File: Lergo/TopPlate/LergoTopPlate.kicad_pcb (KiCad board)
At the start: 2 copper layers, 164 x 146.3 mm, 39 parts, among them SW2 KEY_SWITCH, SW2 PRO MICRO

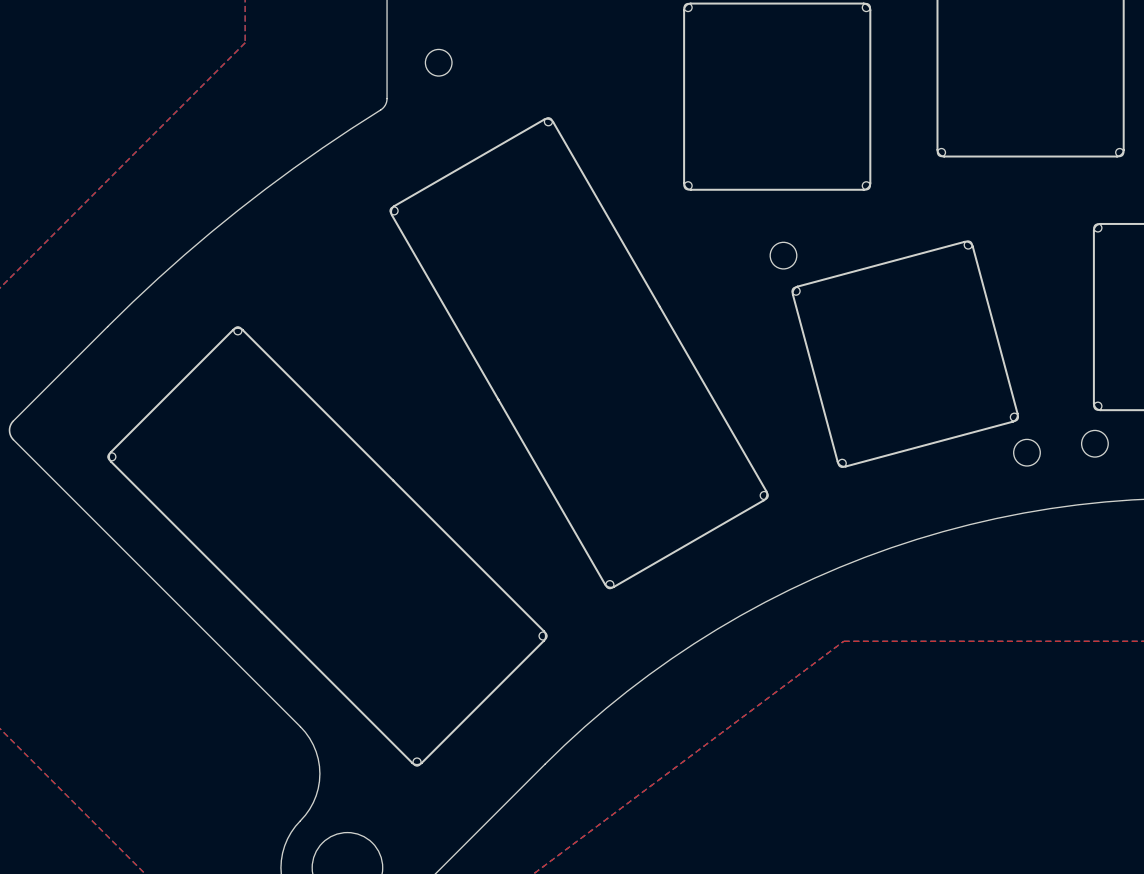
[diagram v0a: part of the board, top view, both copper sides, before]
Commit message: Integrating Pimoroni trackball in all top plates.
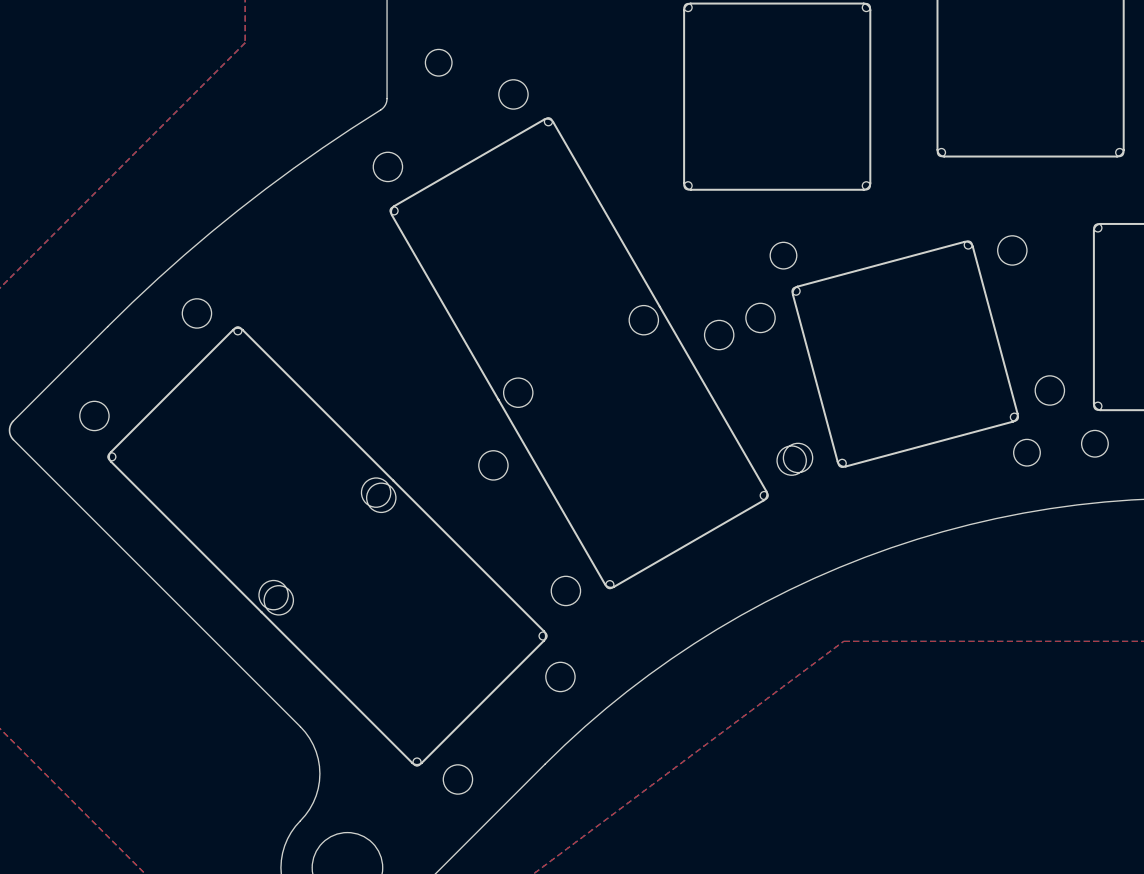
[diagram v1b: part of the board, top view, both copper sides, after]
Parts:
- added REF**: Pimoroni_Trackball, Lergo Footprints:Pimoroni_Trackball, F.Cu at (90.4, 128.6)
- added REF**: Pimoroni_Trackball, Lergo Footprints:Pimoroni_Trackball, F.Cu at (111.3, 112.6)
- added REF**: Pimoroni_Trackball, Lergo Footprints:Pimoroni_Trackball, F.Cu at (103.9, 142.1)
- added REF**: Pimoroni_Trackball, Lergo Footprints:Pimoroni_Trackball, F.Cu at (120.8, 129.1)
- added REF**: Pimoroni_Trackball, Lergo Footprints:Pimoroni_Trackball, F.Cu at (140.6, 120.9)

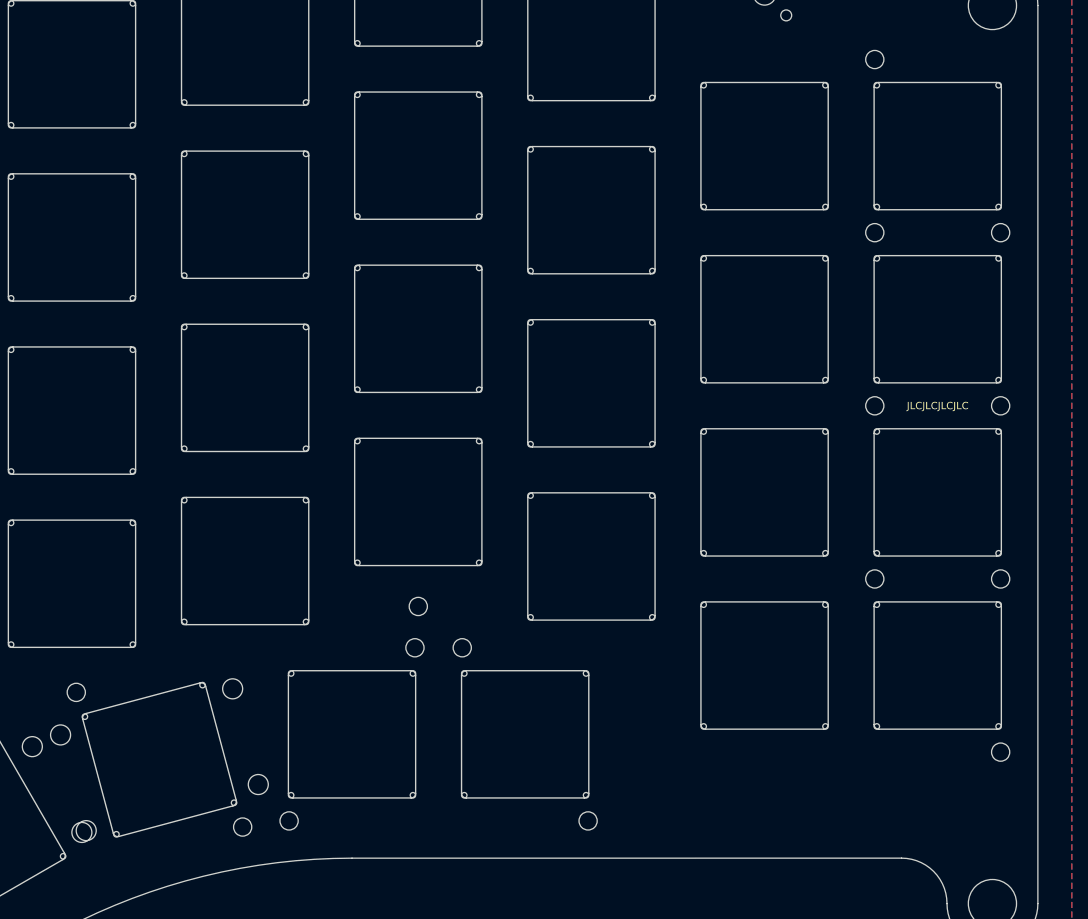
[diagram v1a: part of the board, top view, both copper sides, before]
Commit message: Extended silkscreen for roller encoder on all pre-drilled encoder positions.
Also, doubled the pre-drills rotated 90 degrees for easier mounting of roller encoder in alternate direction.
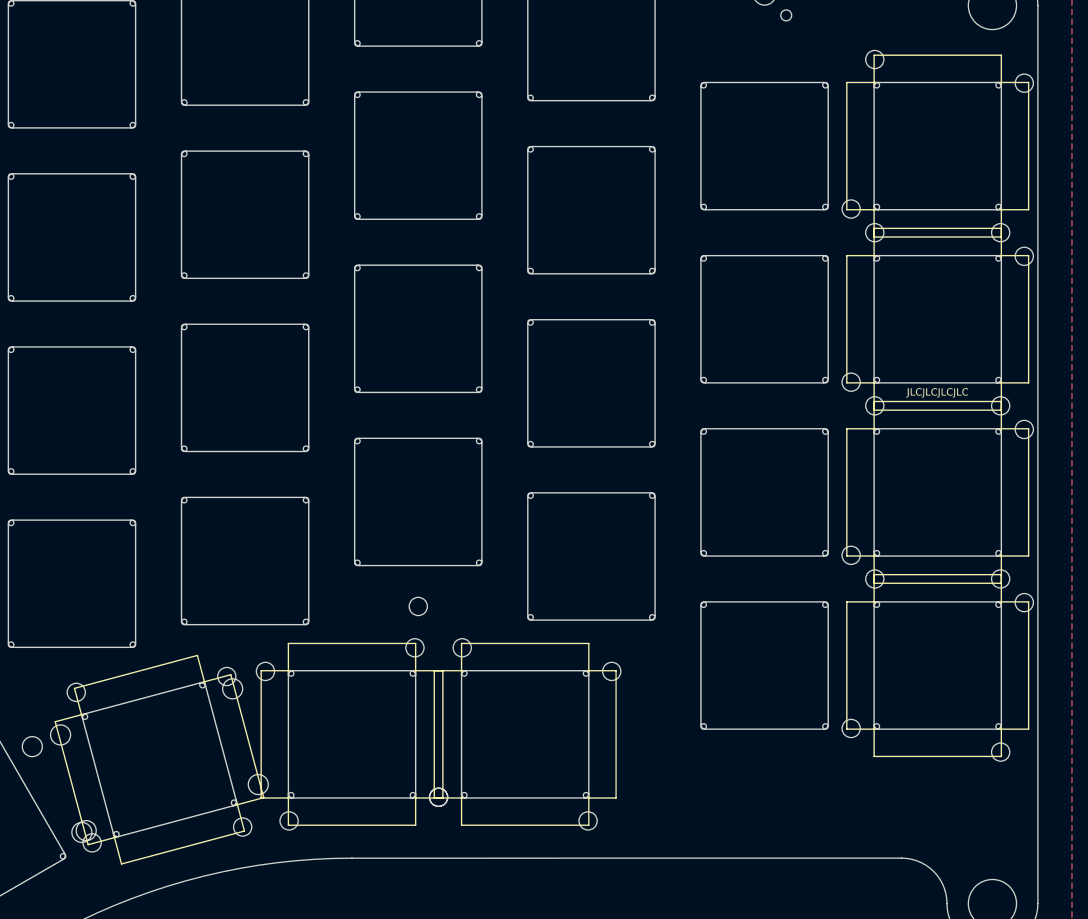
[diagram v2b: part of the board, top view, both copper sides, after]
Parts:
- added REF**: RollerEncoder_Panasonic_EVQWGD001, Lergo Footprints:RollerEncoder_TopPlate, F.Cu at (140.6, 120.9)
- added REF**: RollerEncoder_Panasonic_EVQWGD001, Lergo Footprints:RollerEncoder_TopPlate, F.Cu at (226.2, 53.4)
- added REF**: RollerEncoder_Panasonic_EVQWGD001, Lergo Footprints:RollerEncoder_TopPlate, F.Cu at (226.2, 72.5)
- added REF**: RollerEncoder_Panasonic_EVQWGD001, Lergo Footprints:RollerEncoder_TopPlate, F.Cu at (226.2, 91.5)
- added REF**: RollerEncoder_Panasonic_EVQWGD001, Lergo Footprints:RollerEncoder_TopPlate, F.Cu at (226.2, 110.5)
- added REF**: RollerEncoder_Panasonic_EVQWGD001, Lergo Footprints:RollerEncoder_TopPlate, F.Cu at (161.8, 118.1)
- added REF**: RollerEncoder_Panasonic_EVQWGD001, Lergo Footprints:RollerEncoder_TopPlate, F.Cu at (180.8, 118.1)
- moved JLCJLCJLCJLC 1.50 mm to (226.2, 80.5)
